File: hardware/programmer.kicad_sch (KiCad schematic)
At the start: 11 parts, among them J1 Conn_01x02_Pin, J2 Conn_01x08_Pin, J3 Conn_01x06_Pin, J4 Conn_01x02_Pin, SW1 SW_Push_Dual, SW2 SW_Push_Dual, U2 74HC595, U3 74HC595

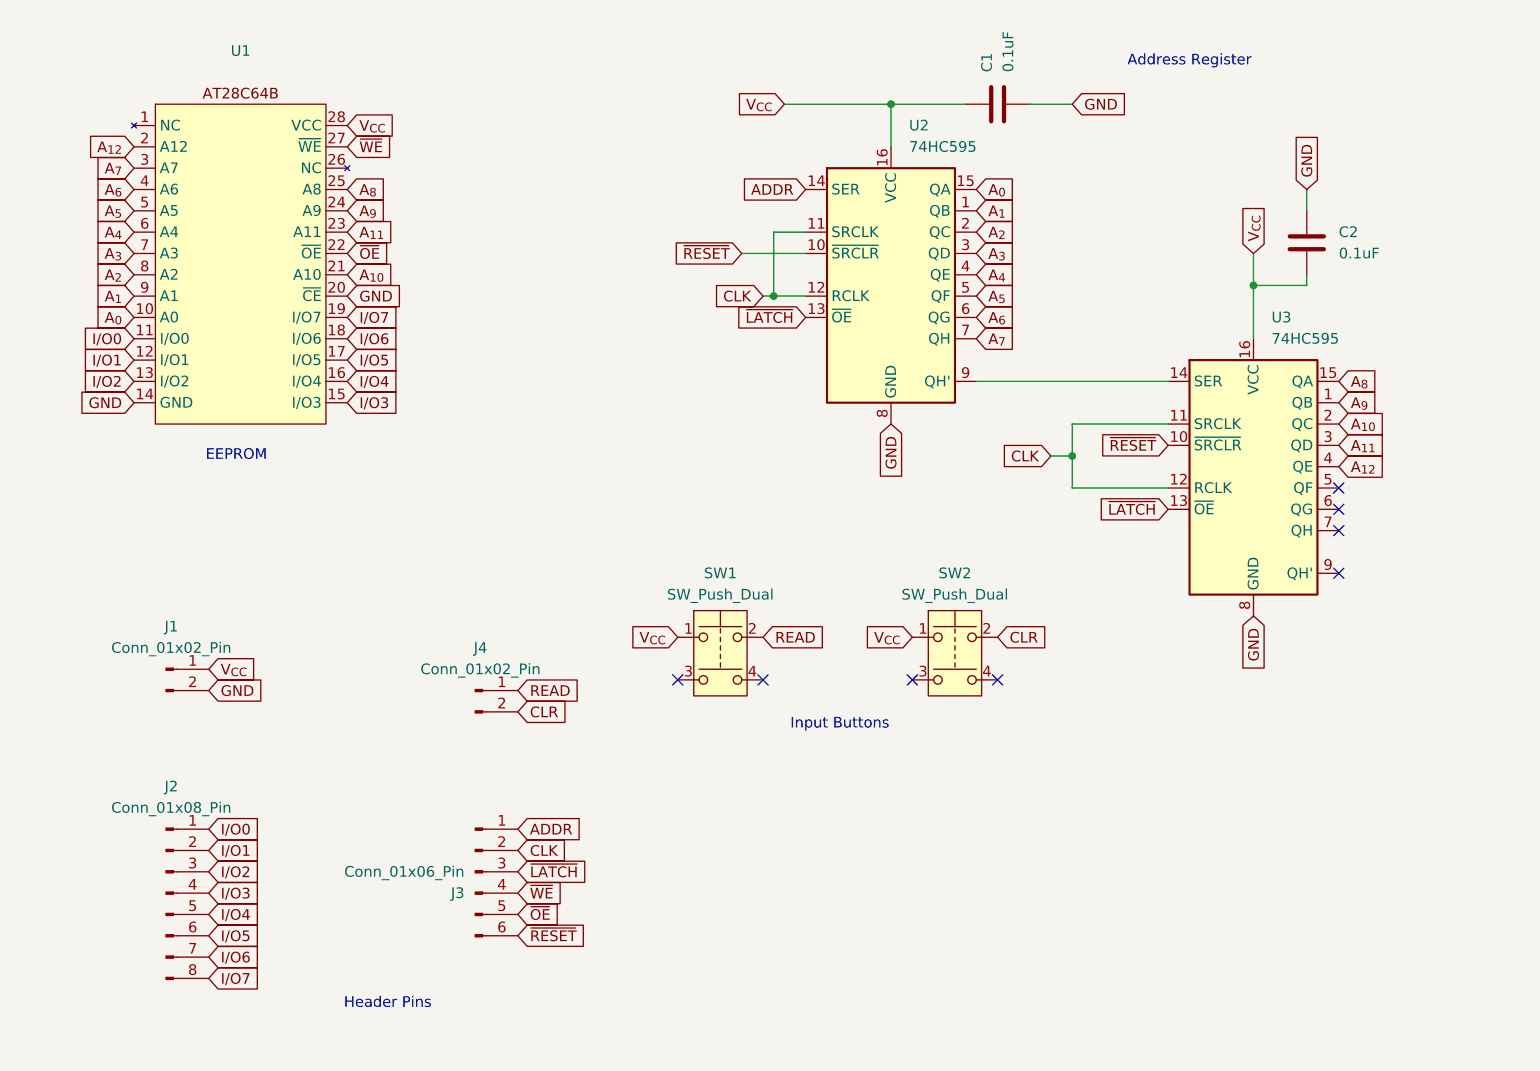
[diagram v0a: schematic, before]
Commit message: modified schematic for system assembly
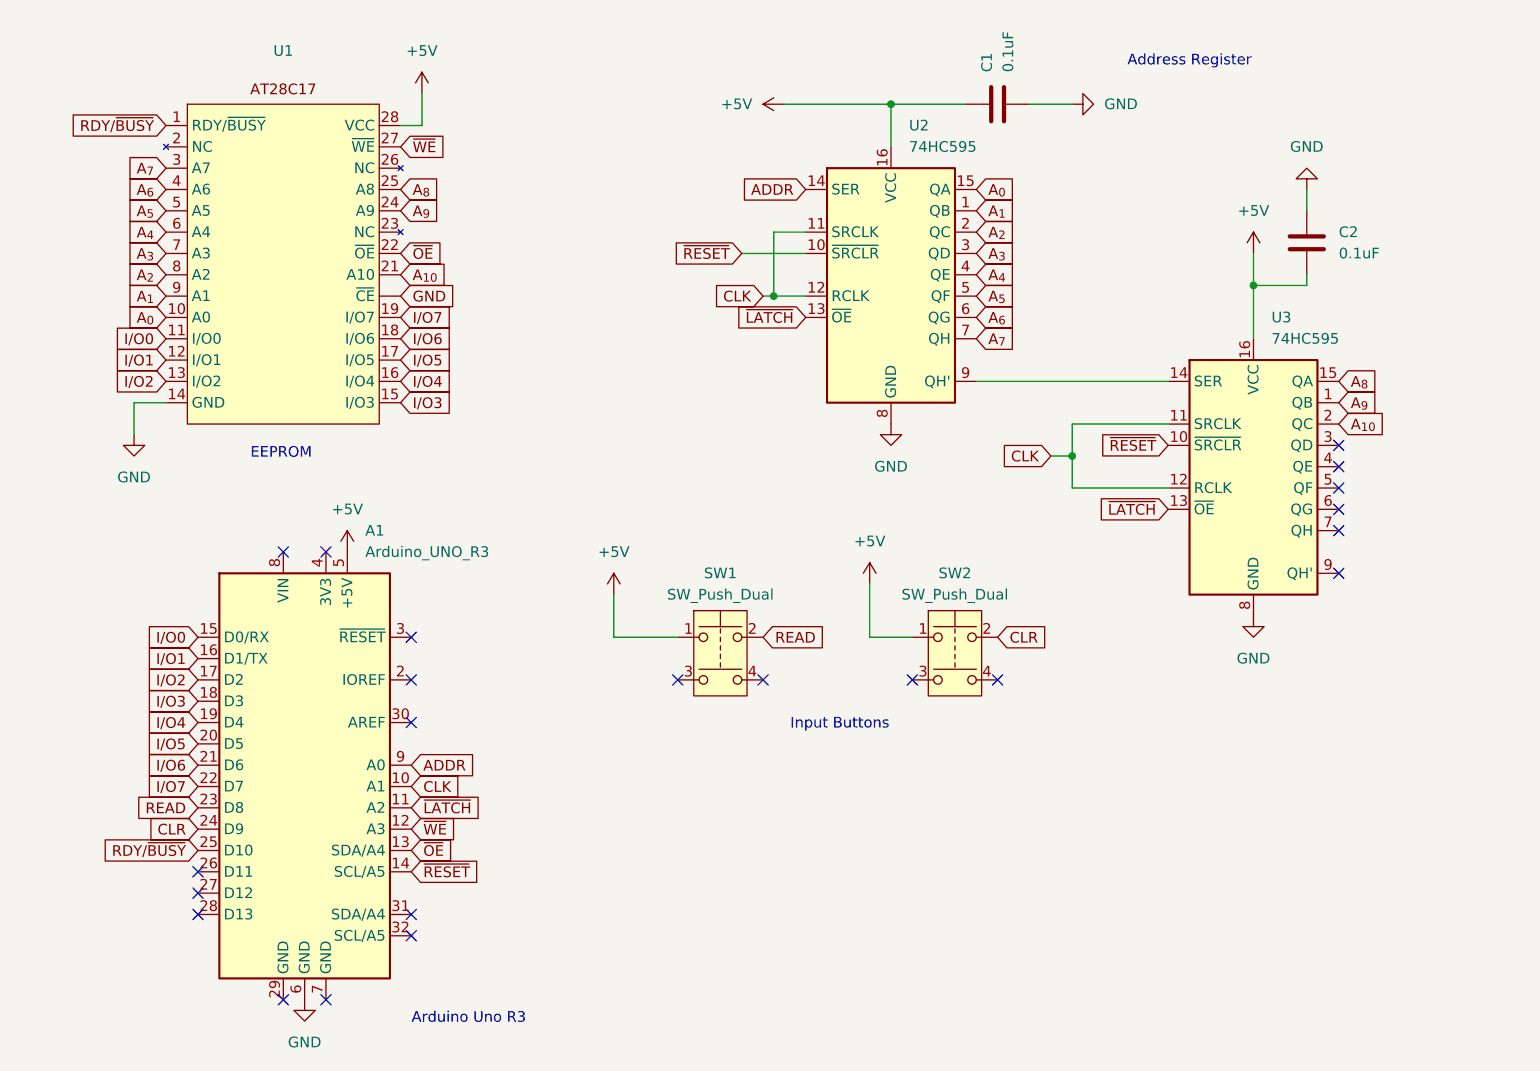
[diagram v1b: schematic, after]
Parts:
- removed J1, J4: Conn_01x02_Pin, Connector_PinHeader_1.27mm:PinHeader_1x02_P1.27mm_Vertical, symbol Connector:Conn_01x02_Pin
- removed J2: Conn_01x08_Pin, Connector_PinHeader_2.54mm:PinHeader_1x08_P2.54mm_Vertical, symbol Connector:Conn_01x08_Pin
- removed J3: Conn_01x06_Pin, Connector_PinHeader_2.54mm:PinHeader_1x06_P2.54mm_Vertical, symbol Connector:Conn_01x06_Pin
- removed U1: ~, Package_DIP:DIP-28_W15.24mm, symbol Memory_EEPROM:AT28C64B
- added A1: Arduino_UNO_R3, Module:Arduino_UNO_R3, symbol MCU_Module:Arduino_UNO_R3
- added U1: ~, symbol Memory_EEPROM:AT28C17
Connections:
- net ADDR: now also A1.9 (A0)
- net A_{0}: now also U1.10 (A0)
- net A_{10}: now also U1.21 (A10)
- net A_{1}: now also U1.9 (A1)
- net A_{2}: now also U1.8 (A2)
- net A_{3}: now also U1.7 (A3)
- net A_{4}: now also U1.6 (A4)
- net A_{5}: now also U1.5 (A5)
- net A_{6}: now also U1.4 (A6)
- net A_{7}: now also U1.3 (A7)
- net A_{8}: now also U1.25 (A8)
- net A_{9}: now also U1.24 (A9)
- net CLK: now also A1.10 (A1)
- net CLR: now also A1.24 (D9)
- net GND: now also A1.6 (GND), U1. (~{CE}), U1.14 (GND)
- net I/O0: now also A1.15 (D0/RX), U1.11 (I/O0)
- net I/O1: now also A1.16 (D1/TX), U1.12 (I/O1)
- net I/O2: now also A1.17 (D2), U1.13 (I/O2)
- net I/O3: now also A1.18 (D3), U1.15 (I/O3)
- net I/O4: now also A1.19 (D4), U1.16 (I/O4)
- net I/O5: now also A1.20 (D5), U1.17 (I/O5)
- net I/O6: now also A1.21 (D6), U1.18 (I/O6)
- net I/O7: now also A1.22 (D7), U1.19 (I/O7)
- net READ: now also A1.23 (D8)
- net ~{LATCH}: now also A1.11 (A2)
- net ~{OE}: now also A1.13 (SDA/A4), U1.22 (~{OE})
- net ~{RESET}: now also A1.14 (SCL/A5)
- net ~{WE}: now also A1.12 (A3), U1.27 (~{WE})
- net A_{11}: no longer names the net of U3.3 (QD)
- net A_{12}: no longer names the net of U3.4 (QE)
- net V_{CC} renamed +5V
- net +5V: now also A1.5 (+5V), U1.28 (VCC)
- new net RDY/~{BUSY}: A1.25 (D10), U1.1 (RDY/~{BUSY})
- no-connect marks 8 -> 22
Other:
- note added: "Arduino Uno R3"
- note removed: "Header Pins"

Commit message: intial firmware
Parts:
- A1: footprint Module:Arduino_UNO_R3 -> shield-headers:eeprom_programmer
- U1: footprint (none) -> DIP28 _Socket:CONN_110-99-328-41-001000_MIM
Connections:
- net GND: now also U1.20 (~{CE}); no longer U1. (~{CE})
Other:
- moved on the sheet: C1, C2, U2, U3
